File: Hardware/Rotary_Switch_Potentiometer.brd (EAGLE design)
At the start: 43.2 x 25.4 mm, 16 parts, among them SW1 1x10

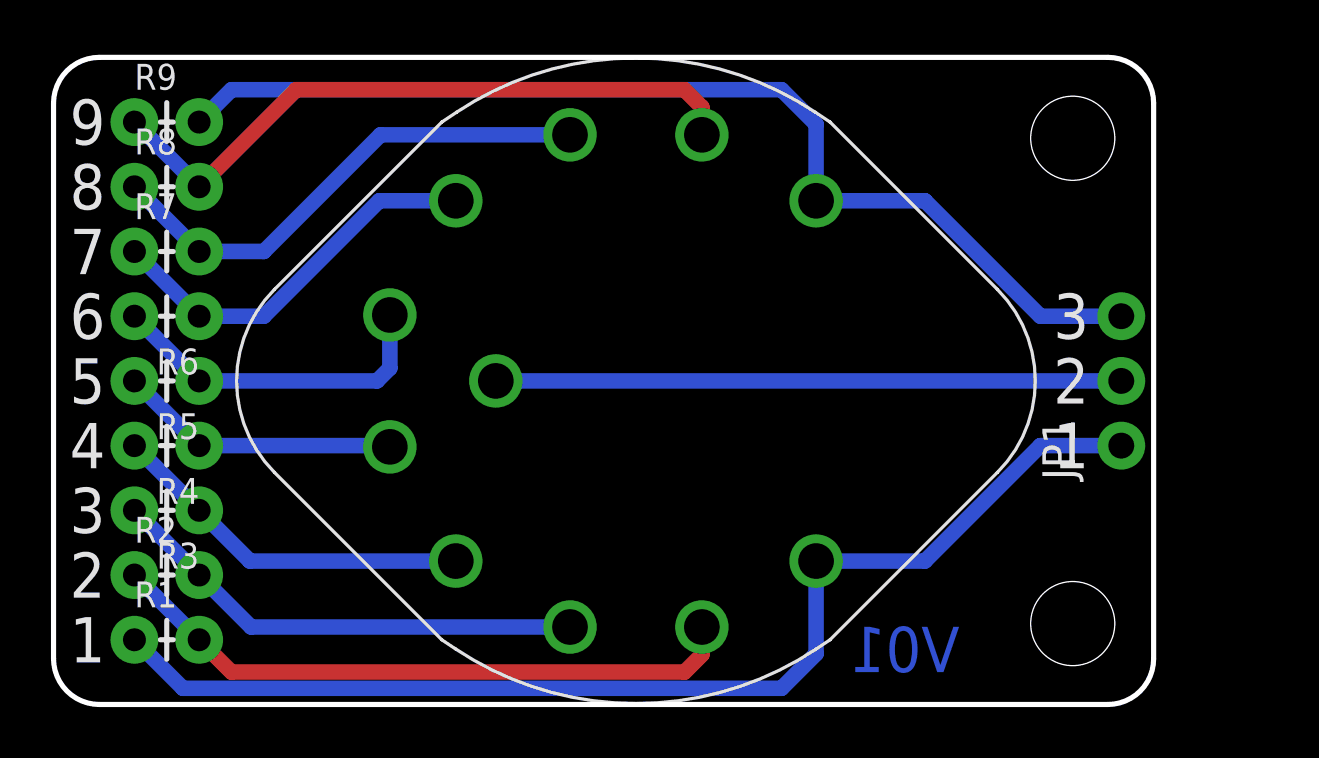
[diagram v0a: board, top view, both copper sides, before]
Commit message: Updates from working with protos.
Now has 4 mounting holes.
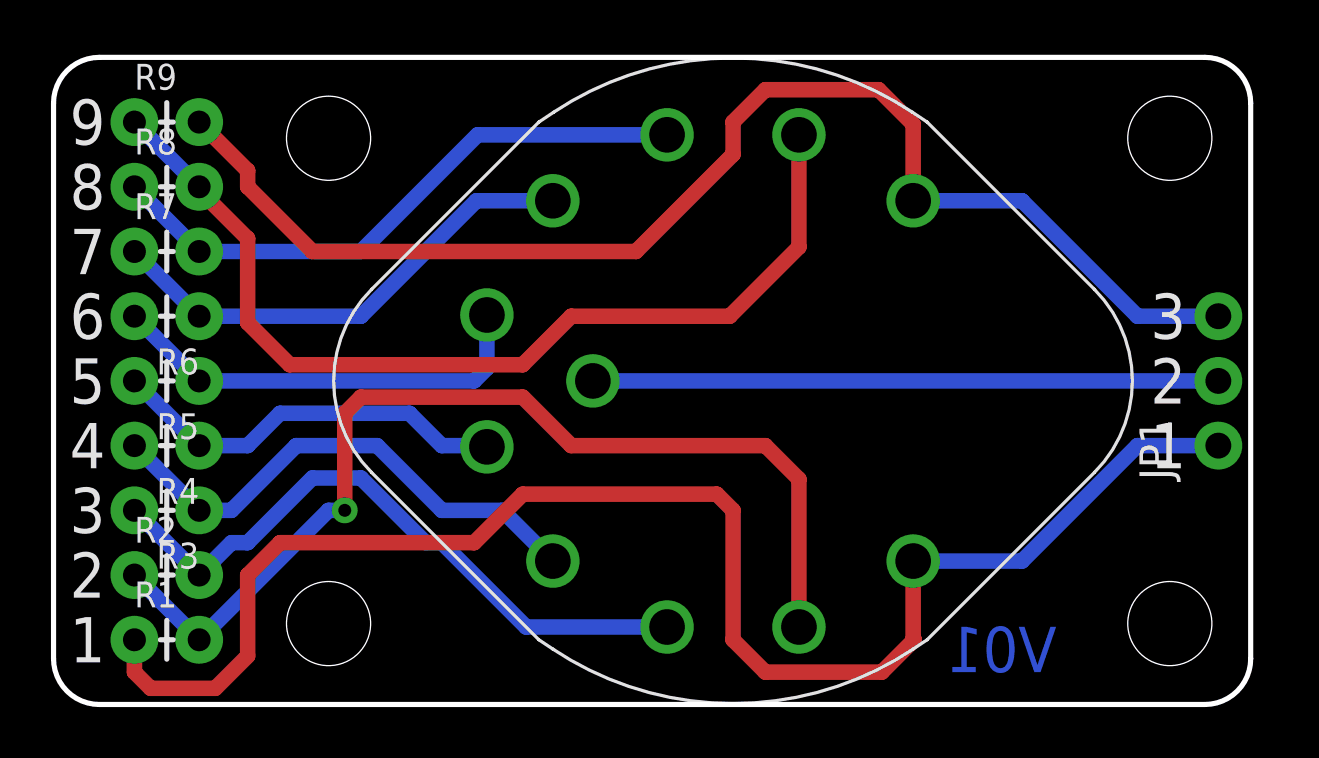
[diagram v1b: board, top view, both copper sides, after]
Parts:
- added STANDOFF5, STANDOFF6: STAND-OFF, SparkFun-Electromechanical:STAND-OFF
- moved JP1 3.81 mm to (45.7, 10.2)
- moved LOGO1 3.81 mm to (26.7, 10.2)
- moved LOGO3 3.81 mm to (33.0, 3.81)
- moved SW1 3.81 mm to (26.7, 12.7)
- moved STANDOFF1 3.81 mm to (43.8, 3.17)
- moved STANDOFF2 3.81 mm to (43.8, 22.2)
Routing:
- net N$5: track 25.2 -> 40.4 mm, vias 0 -> 1
- net N$2: track 45.6 -> 60.5 mm
- net N$11: track 26.3 -> 38.4 mm
- net N$3: track 42.2 -> 51.3 mm
- net N$6: track 19.0 -> 26.0 mm
- net N$7: track 14.5 -> 20.4 mm
- net N$8: track 11.1 -> 16.0 mm
- net N$9: track 13.4 -> 17.2 mm
- net N$10: track 15.5 -> 19.4 mm
- net N$4: track 20.0 -> 23.9 mm
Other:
- board size 43.2 x 25.4 mm -> 47 x 25.4 mm

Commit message: Tweaks after engineering group review.
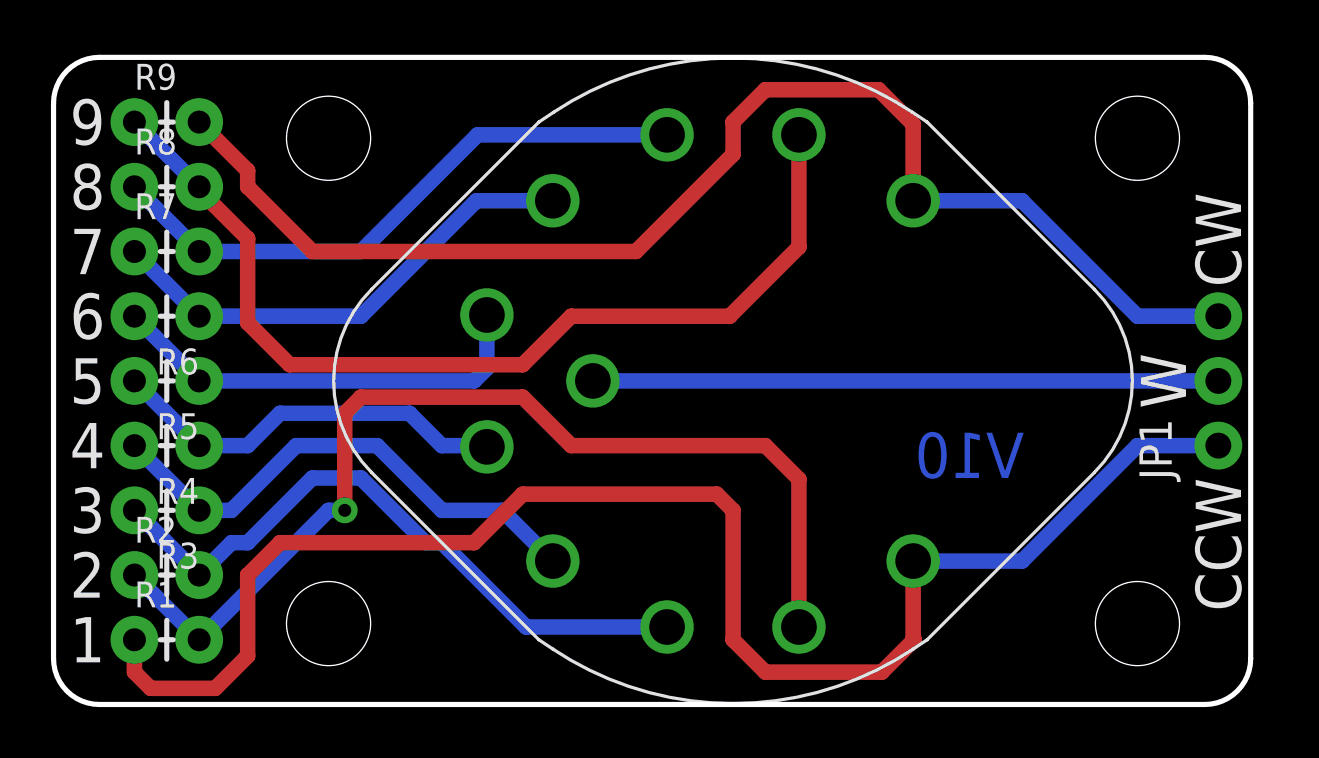
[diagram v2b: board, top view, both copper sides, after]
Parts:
- moved FRAME1 6.35 mm to (0.00, -14.0)
- moved STANDOFF1 1.27 mm to (42.5, 3.17)
- moved STANDOFF2 1.27 mm to (42.5, 22.2)
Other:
- board text added: "0.35 diam panel hole"
- board text added: "4x 0.13 diam."
- board text added: "All units in Inches"
- board text added: "CCW"
- board text added: "CW"
- board text added: "V10"
- board text added: "W"
- board text removed: "V01"
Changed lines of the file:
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@@
 <drawing>
 <settings>
-<setting alwaysvectorfont="no"/>
+<setting alwaysvectorfont="yes"/>
 <setting verticaltext="up"/>
 </settings>
@@
 <wire x1="1.79605" y1="0" x2="45.19395" y2="0" width="0.2032" layer="20"/>
 <wire x1="45.19395" y1="0" x2="46.99" y2="1.79605" width="0.2032" layer="20" curve="90"/>
-<text x="30.48" y="-7.62" size="1.778" layer="51" font="vector" ratio="15">Byron Jacquot</text>
-<text x="44.45" y="10.16" size="1.778" layer="21" font="vector" ratio="15" rot="R180" align="center-left">1</text>
-<text x="44.45" y="12.7" size="1.778" layer="21" font="vector" ratio="15" rot="R180" align="center-left">2</text>
-<text x="44.45" y="15.24" size="1.778" layer="21" font="vector" ratio="15" rot="R180" align="center-left">3</text>
+<text x="30.48" y="-13.97" size="1.778" layer="51" font="vector" ratio="15">Byron Jacquot</text>
+<text x="45.72" y="8.89" size="1.778" layer="21" font="vector" ratio="15" rot="R270" align="center-left">CCW</text>
+<text x="44.45" y="12.7" size="1.778" layer="21" font="vector" ratio="15" rot="R90" align="bottom-center">W</text>
+<text x="45.72" y="16.383" size="1.778" layer="21" font="vector" ratio="15" rot="R90" align="center-left">CW</text>
 <text x="27.94" y="18.415" size="1.778" layer="22" font="vector" ratio="15" rot="MR0" align="top-center">Rotary Switch
 Potentiometer</text>
@@
 <text x="0.635" y="20.32" size="1.778" layer="21" font="vector" ratio="15" align="center-left">8</text>
 <text x="0.635" y="22.86" size="1.778" layer="21" font="vector" ratio="15" align="center-left">9</text>
-<text x="42.545" y="10.16" size="1.778" layer="22" font="vector" ratio="15" rot="MR180" align="center-left">1</text>
-<text x="42.545" y="12.7" size="1.778" layer="22" font="vector" ratio="15" rot="MR180" align="center-left">2</text>
-<text x="42.545" y="15.24" size="1.778" layer="22" font="vector" ratio="15" rot="MR180" align="center-left">3</text>
 <text x="1.905" y="2.54" size="1.778" layer="22" font="vector" ratio="15" rot="MR0" align="center-left">1</text>
 <text x="1.905" y="5.08" size="1.778" layer="22" font="vector" ratio="15" rot="MR0" align="center-left">2</text>
@@
 <text x="1.905" y="20.32" size="1.778" layer="22" font="vector" ratio="15" rot="MR0" align="center-left">8</text>
 <text x="1.905" y="22.86" size="1.778" layer="22" font="vector" ratio="15" rot="MR0" align="center-left">9</text>
-<text x="39.37" y="1.27" size="1.778" layer="16" font="vector" ratio="15" rot="MR0">V01</text>
+<text x="38.1" y="8.89" size="1.778" layer="16" font="vector" ratio="15" rot="MR0">V10</text>
+<dimension x1="0" y1="0" x2="0" y2="25.4" x3="-15.24" y3="12.7" textsize="1.778" textratio="15" layer="47" unit="inch"/>
+<dimension x1="0" y1="25.4" x2="46.99" y2="25.4" x3="23.495" y3="40.64" textsize="1.778" textratio="15" layer="47" unit="inch" precision="3"/>
+<dimension x1="0" y1="25.4" x2="42.545" y2="25.4" x3="21.2725" y3="36.83" textsize="1.778" textratio="15" layer="47" unit="inch" precision="3"/>
+<dimension x1="0" y1="25.4" x2="26.67" y2="25.4" x3="13.335" y3="33.020003125" textsize="1.778" textratio="15" layer="47" unit="inch"/>
+<dimension x1="0" y1="25.4" x2="10.795" y2="25.4" x3="5.3975" y3="29.210003125" textsize="1.778" textratio="15" layer="47" unit="inch" precision="3"/>
+<dimension x1="0" y1="0" x2="0" y2="3.175" x3="-2.54" y3="1.5875" textsize="1.778" textratio="15" layer="47" unit="inch" precision="3"/>
+<dimension x1="0" y1="0" x2="0" y2="22.225" x3="-11.43" y3="11.1125" textsize="1.778" textratio="15" layer="47" unit="inch" precision="3"/>
+<dimension x1="0" y1="0" x2="0" y2="12.7" x3="-7.62" y3="6.35" textsize="1.778" textratio="15" layer="47" unit="inch" precision="3"/>
+<text x="5.08" y="-5.08" size="1.778" layer="47" font="vector" ratio="15">All units in Inches</text>
+<circle x="26.67" y="12.7" radius="4.445" width="0.254" layer="47"/>
+<dimension x1="42.545" y1="22.225" x2="50.8" y2="26.67" x3="54.61" y3="26.67" textsize="1.778" textratio="15" layer="47" dtype="leader" unit="inch"/>
+<text x="54.61" y="26.67" size="1.778" layer="47" font="vector" ratio="15">4x 0.13 diam.</text>
+<dimension x1="26.67" y1="12.7" x2="38.1" y2="-3.81" x3="44.45" y3="-3.81" textsize="1.778" textratio="15" layer="47" dtype="leader" unit="inch"/>
+<text x="44.45" y="-3.81" size="1.778" layer="47" font="vector" ratio="15">0.35 diam panel hole</text>
+<text x="45.72" y="16.383" size="1.778" layer="22" font="vector" ratio="15" rot="MR90" align="center-left">CW</text>
+<text x="44.45" y="12.7" size="1.778" layer="22" font="vector" ratio="15" rot="MR270" align="bottom-center">W</text>
+<text x="45.72" y="8.89" size="1.778" layer="22" font="vector" ratio="15" rot="MR270" align="center-left">CCW</text>
 </plain>
 <attributes>
@@
 </autorouter>
 <elements>
-<element name="FRAME1" library="SparkFun-Aesthetics" package="CREATIVE_COMMONS" value="FRAME-LETTER" x="0" y="-7.62"/>
+<element name="FRAME1" library="SparkFun-Aesthetics" package="CREATIVE_COMMONS" value="FRAME-LETTER" x="0" y="-13.97"/>
 <element name="SW1" library="SparkFun-Electromechanical" package="ROTARY_SWITCH_1X10_KIT" value="1x10" x="26.67" y="12.7" rot="R270">
 <attribute name="PROD_ID" value="SWCH-12120" x="10.16" y="-13.97" size="1.778" layer="27" rot="R270" display="off"/>
 </element>
 <element name="LOGO1" library="SparkFun-Aesthetics" package="OSHW-LOGO-M" value="OSHW-LOGOM" x="26.67" y="10.16" rot="MR0"/>
-<element name="STANDOFF1" library="SparkFun-Electromechanical" package="STAND-OFF" value="STAND-OFF" x="43.815" y="3.175"/>
-<element name="STANDOFF2" library="SparkFun-Electromechanical" package="STAND-OFF" value="STAND-OFF" x="43.815" y="22.225"/>
+<element name="STANDOFF1" library="SparkFun-Electromechanical" package="STAND-OFF" value="STAND-OFF" x="42.545" y="3.175"/>
+<element name="STANDOFF2" library="SparkFun-Electromechanical" package="STAND-OFF" value="STAND-OFF" x="42.545" y="22.225"/>
 <element name="LOGO3" library="SparkFun-Aesthetics" package="SFE_LOGO_NAME_.1" value="SFE_LOGO_NAME.1_INCH" x="33.02" y="3.81" rot="MR0"/>
 <element name="JP1" library="SparkFun-Connectors" package="1X03_NO_SILK" value="" x="45.72" y="10.16" rot="R90"/>
